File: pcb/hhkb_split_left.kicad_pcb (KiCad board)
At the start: 2 copper layers, 140.4 x 97.4 mm, 74 parts, among them SW1 Esc, SW10 E, SW11 R, SW12 T, SW13 Ctrl, SW14 A, SW15 S, SW16 D, SW17 F, SW18 G, SW19 Shift, SW2 1, SW20 Z, SW21 X, SW22 C, SW23 V, SW24 B, SW25 Alt, SW26 Meta, SW27 L-Space, SW3 2, SW4 3, SW5 4, SW6 5, SW7 Tab, SW8 Q, SW9 W, U1 74LVC595

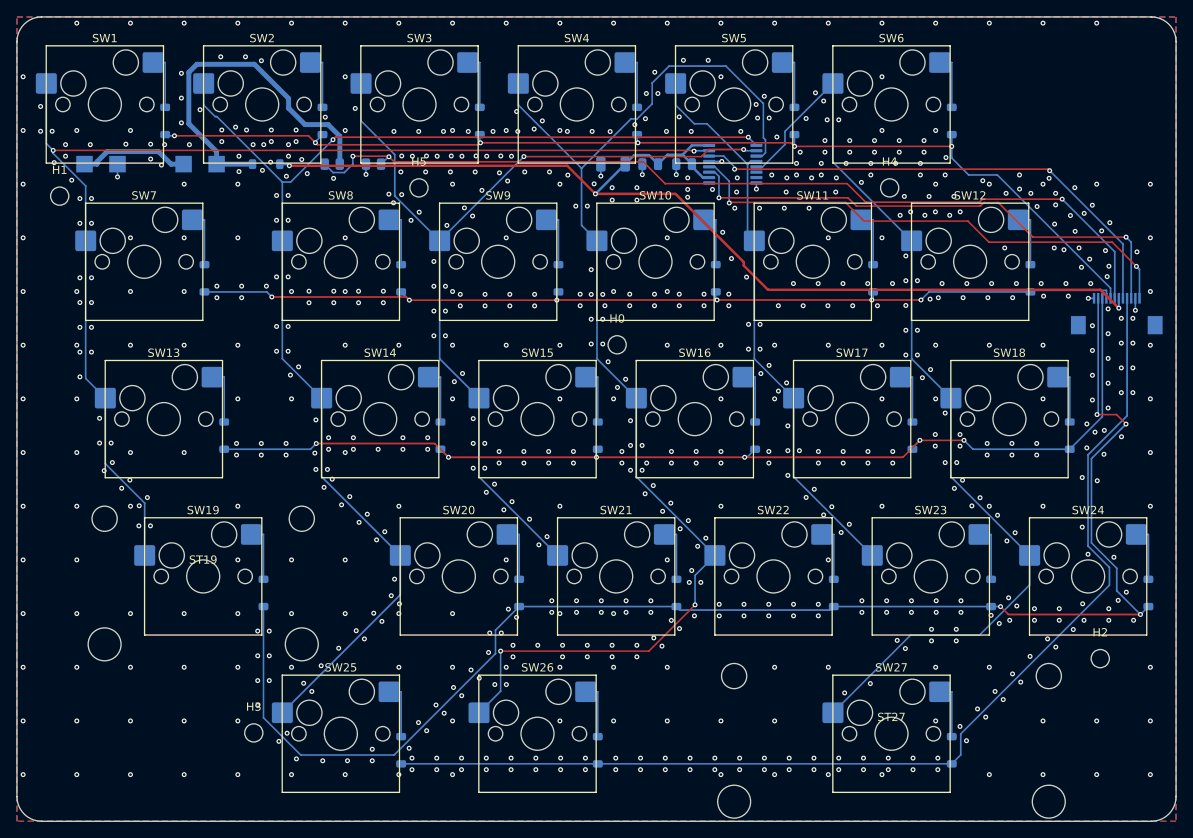
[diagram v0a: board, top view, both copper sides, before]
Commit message: C_RAIL を消した。置き場所の根拠が持たず C_U1 の重複だった
open-gaps #39 は「U1 の隣か J_DB の隣か」で止まっていたが、二択の
立て方が違った。FFC の反対側の C_DB を数えると、U_MCU から 3.95mm の
XIAO 用パスコンで、FFC 入口ではない。つまりケーブル入口のパスコンは
もともと両端どちらにも無く、片端だけ手当てする案は理屈が対称にならない。

C_RAIL は実測で J_DB から 70mm、C_U1 の 5.1mm 隣にあった（J_DB を
帯 1 へ移したときに取り残された）。名前どおりの役目は果たしていない。

消した理由は「不要と証明できたから」ではなく、必要と言える根拠が
1 つも無く、各 IC が既に自分の直近パスコンを持つから（595 は
C_U1/C_U2、XIAO は C_DB、レールは C_BULK）。

DRC 違反は左右子とも 0 のまま。右だけ未配線が 0 → 1 に増えた。中身は
信号線ではなく、(152.65, 68.37) の GND スティッチングビアがベタから
浮いたもの（C_RAIL の跡地）。自動配線 2 回で同じなので構造的。
配線に大きな変更が控えているため、それと併せて確認する（open-gaps #40）。

⚠️ pytest tools は最後まで通していない。次の配線変更とまとめて回す。

Co-Authored-By: Claude Opus 5 (1M context) <noreply@anthropic.com>
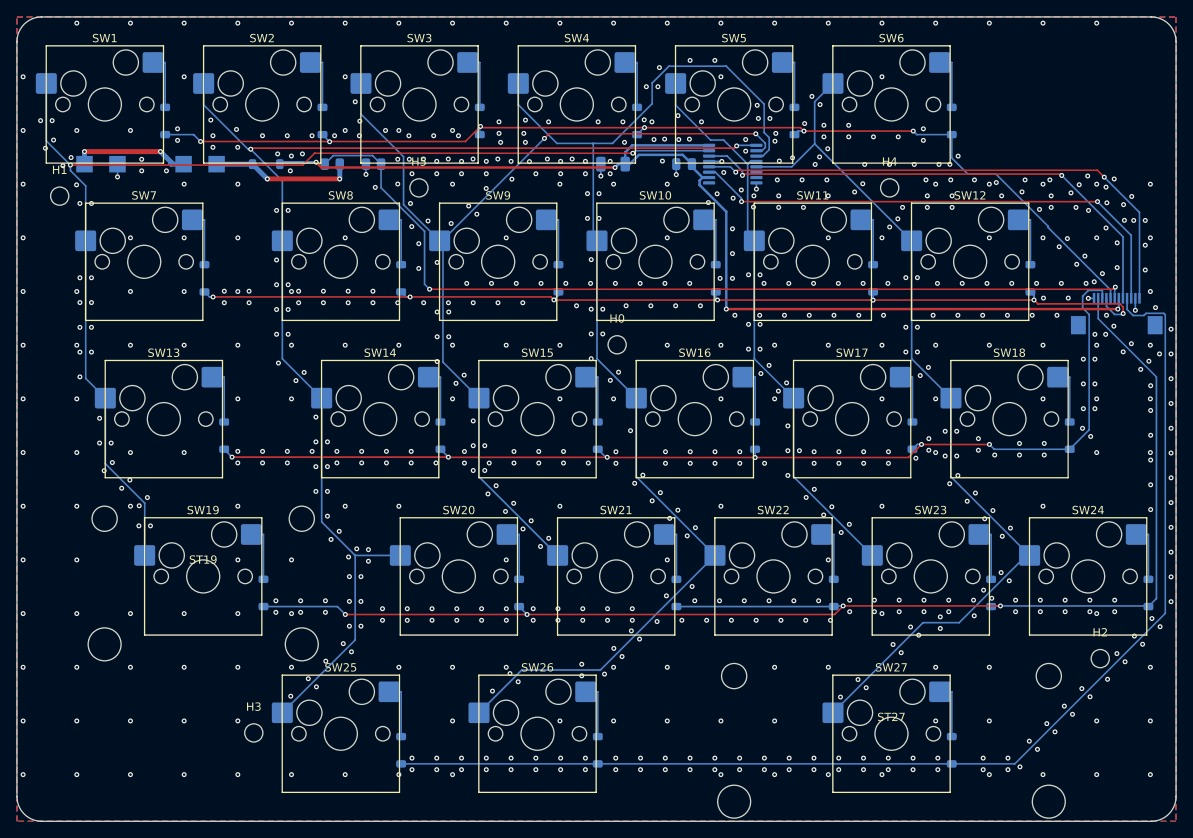
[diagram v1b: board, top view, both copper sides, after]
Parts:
- removed C_RAIL: cap_100n, C_0805_2012Metric
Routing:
- net VBATT_SW: track 43.2 -> 17.4 mm, vias 0 -> 2
- net ROW4: track 134.0 -> 142.7 mm
- net ROW3: track 178.1 -> 171.4 mm
- net COL5: track 115.2 -> 108.6 mm
- net ROW1: track 115.6 -> 122.0 mm, vias 6 -> 7
- net COL3: track 146.2 -> 141.6 mm, vias 2 -> 0
- net COL2: track 110.0 -> 113.9 mm
- net CS: track 62.4 -> 65.0 mm
- net COL1: track 152.2 -> 154.5 mm
- net ROW2: track 130.1 -> 132.4 mm
- net COL0: track 141.6 -> 140.1 mm
- net GND: track 11.2 -> 9.96 mm, vias 817 -> 816
- net SPI_SCK: track 63.3 -> 62.1 mm
- net VBATT_RAW: track 13.4 -> 14.3 mm, vias 0 -> 2
- net SPI_MOSI: track 61.3 -> 62.0 mm
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
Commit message: バルクを子基板へ移し、電源鎖を消費側へ寄せ、行バスを直線にした
利用者の指摘を順に潰した。どれも「測ったら前提が違っていた」型。

1. バルク（C_BULK）を子基板へ
   守る相手は XIAO の µs 級の電流変動（electrical-design 1-5）で、
   595 でも整流点でもない。XIAO は子基板にいるので、主基板に置くと
   FFC 100mm のインダクタンスの外側から供給することになる。
   XIAO の 3V3 パッドから 2.04mm の位置へ移した。

2. 電源ブロックを V3V3 の消費側へ
   整流点 D_PWR が板の左端にあるのに、消費側（C_U1・U1・J_DB）は
   全部反対側だった。U1 の左へ寄せて V3V3 の銅 132→81mm、
   VBATT_SENSE 110→78mm。左の帯 0 はアンテナ禁止域と取付穴で
   分断されていて、プラス側へは出せない（一度出して DRC 13 件）。

3. 行のバスを裏面の直線で自分で引く（prewire_row_bus）
   ROW0 が 222mm・ビア 7 本・区間 54 で表裏を行き来していた。
   同じ行のダイオードの K 側は y が完全に一致し、ライン上に
   スルーホールが無いので直線が引ける（ROW4 は元から 0 ビアだった）。
   左の未配線 1 本（ROW2）はこれで解決した。
   ⚠️ DSN に (autoroute_settings) を足す道は駄目。左が 66 本に壊れた。

4. アンテナの禁止域（30x15mm）を削除
   利用者の「本当にアンテナの真上ですか」で測ったら、覆っていなかった。
     禁止域 y 30.60..45.60 / 基板後端 48.70 / アンテナ 49.50..53.00
   アンテナは基板の後端より 0.80mm 奥（XIAO_OVERHANG 1.8mm の効果）で、
   平面的に基板の外。禁止域は 3.9mm 的を外したまま 450mm² を捨て、
   左の配線を圧迫していた。
   **根拠に挙げられていた検査は存在しなかった。**interface.py は
   test_the_antenna_keepout_actually_covers_the_antenna が照合すると
   書いていたが、その名前の検査はどこにも無い。実在したのは
   「禁止域の中が空か」だけで、位置は誰も見ていなかった。
   代わりに test_the_antenna_clears_the_main_board を置いた
   （XIAO_OVERHANG を 0 にすると落ちることを確認済み）。

   → open-gaps #23 の幾何の証明（アンテナは必ず 4mm 以上 基板の下に
     入る）は、もう成立していない。ただし余裕は 0.80mm しかないので、
     手 0（アルミ箔で RSSI）の価値は残る。#23 の書き直しは次。

残っているもの（次に着手する）:
  右 未配線 3（GND 離島 1 + V3V3 が J_DB へ届かない 2）★機能的な故障
  左 未配線 1（GND 離島）
  違反はどれも 0。自前配線で塞ぐ案は取らない——今は綺麗に引けても
  配置を変えると黙って壊れ、再現性が無い（利用者の判断）。

pytest tools は未実行。

Co-Authored-By: Claude Opus 5 (1M context) <noreply@anthropic.com>
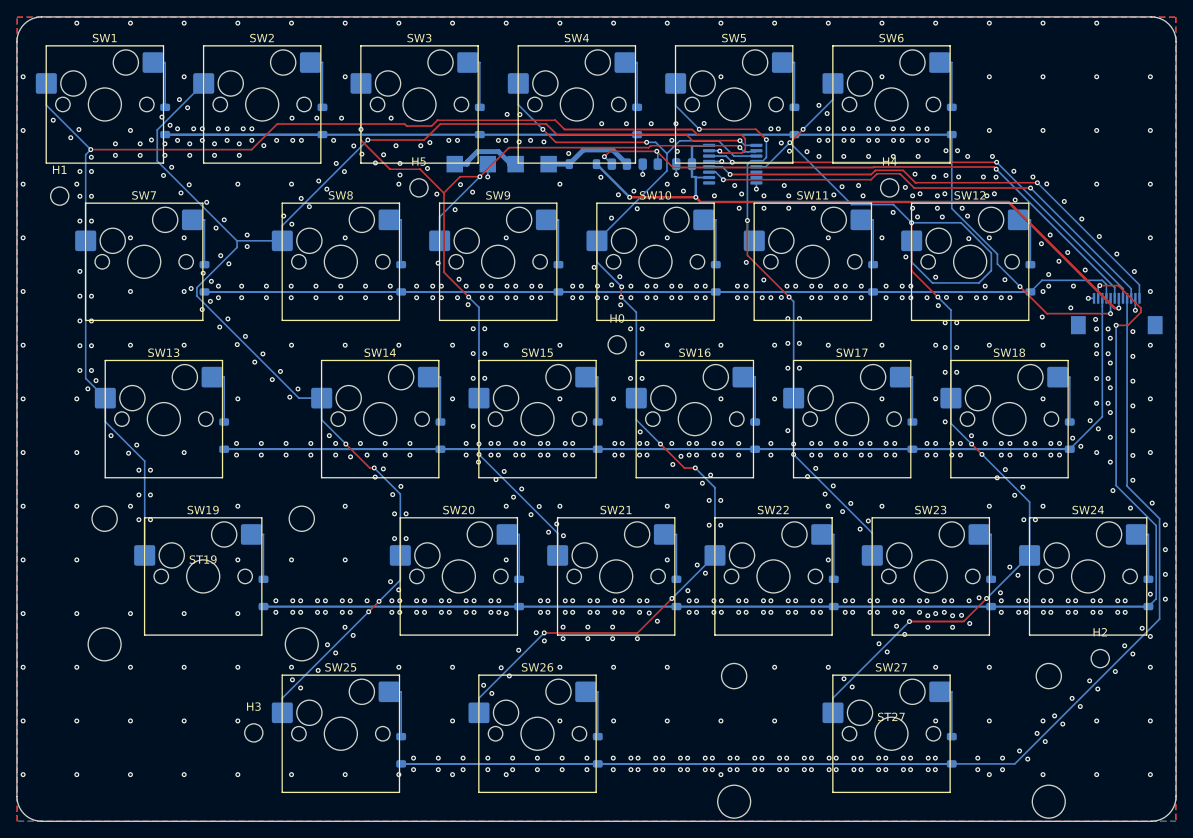
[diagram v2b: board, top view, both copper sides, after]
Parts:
- removed C_BULK: cap_100u, C_1206_3216Metric
- moved BT1_+ 44.8 mm to (132.8, 69.1)
- moved BT1_- 44.8 mm to (136.8, 69.1)
- moved SW_PWR_1 40.2 mm to (140.2, 69.1)
- moved SW_PWR_2 40.2 mm to (144.2, 69.1)
- moved D_PWR 38.3 mm to (148.3, 69.1)
- moved R_HI 34.8 mm to (152.8, 69.1)
- moved R_LO 33.5 mm to (156.5, 69.1)
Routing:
- net ROW0: track 131.4 -> 245.6 mm, vias 6 -> 2
- net ROW2: track 132.4 -> 224.7 mm, vias 6 -> 0
- net ROW3: track 171.4 -> 262.7 mm, vias 4 -> 2
- net ROW1: track 122.0 -> 211.7 mm, vias 7 -> 0
- net ROW4: track 142.7 -> 206.3 mm
- net V3V3: track 132.4 -> 82.1 mm, vias 4 -> 3
- net VBATT_SENSE: track 109.8 -> 73.1 mm, vias 2 -> 3
- net COL5: track 108.6 -> 139.5 mm, vias 0 -> 8
- net COL1: track 154.5 -> 173.5 mm, vias 2 -> 6
- net COL0: track 140.1 -> 150.5 mm
- net COL3: track 141.6 -> 131.7 mm, vias 0 -> 8
- net COL4: track 69.1 -> 76.6 mm, vias 0 -> 6
- net VBATT_SW: track 17.4 -> 10.9 mm, vias 2 -> 0
- net COL2: track 113.9 -> 119.5 mm, vias 2 -> 6
- net VBATT_RAW: track 14.3 -> 8.91 mm, vias 2 -> 0
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
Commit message: VBATT_RAW を廃止し、V3V3 を FFC の隙間を通る幅に直した
1. 電池の + を基板に通さない（利用者の指摘）
   BT1.+ →(VBATT_RAW)→ SW_PWR.1 と基板を往復させていたが、電池
   ボックスもスイッチもリード線で繋ぐので、+ はスイッチへ直接
   はんだ付けすればよい。線 4→3 本・ランド 4→2 個。基板から
   VBATT_RAW というネットが丸ごと消えた。
   ランドの数は WIRE_PAD_KINDS で 2 に決め打ちしていたのを、
   宣言した端子の数から取るように直した。参照名の接尾辞は端子数に
   関わらず付ける（1 個になった瞬間に BT1 へ化けて board_refs と
   回路図の配置表が一斉にずれるため）。

2. V3V3 の線幅 0.3 → 0.2mm ★右の V3V3 断線の真因
   「FFC の 0.30mm パッドに届く必要がある」と書いてあったが、
   **パッドの幅とパッドの隙間を取り違えていた。**0.5mm ピッチ・
   パッド幅 0.30 の列を幅 0.30 で抜けると隣のパッドまで 0.200mm
   ちょうどで、丸めで即割る（0.20mm なら 0.250mm で通る）。
   右基板で V3V3 だけが J_DB から出られず、自動配線器がビアだけ
   (72.75, 84.00) に置いて両端とも繋がず放棄していた。同じ列の
   VBATT_SENSE・SPI_MOSI・SCK・CS は全部 0.20mm で脱出できていた。
   電流は BLE のパルスで 15mA、バルクは子基板側なのでこの線が
   運ぶのは平均電流だけ。0.20mm でも桁が違うほど余る。

3. DSN のクリアランスマージン 15 → 20µm
   上の変更のあと 15 では丸め不足が顕在化し、違反が左 1・右 3 出た
   （実測 0.1917〜0.1919mm ＜ 0.2000mm）。20 で全部消える。
   15/20/25 の結果は autoroute.py に表で残した。

結果:
  左  違反 0 / 未配線 2
  右  違反 0 / 未配線 0   ← 今日はじめて 0/0
  子  違反 0 / 未配線 0

左の 2 本は ROW3/ROW4 が J_DB へ降りる枝。**瑣末と判断**（利用者）。
J_DB の ROW パッドの並び（ROW3,ROW2,ROW1,ROW0,ROW4）が行バスの
y 順と食い違っていて交差する。XIAO のピン割り当てを変えて順序を
揃えれば解ける見込み——次の課題。

pytest tools は未実行。

Co-Authored-By: Claude Opus 5 (1M context) <noreply@anthropic.com>
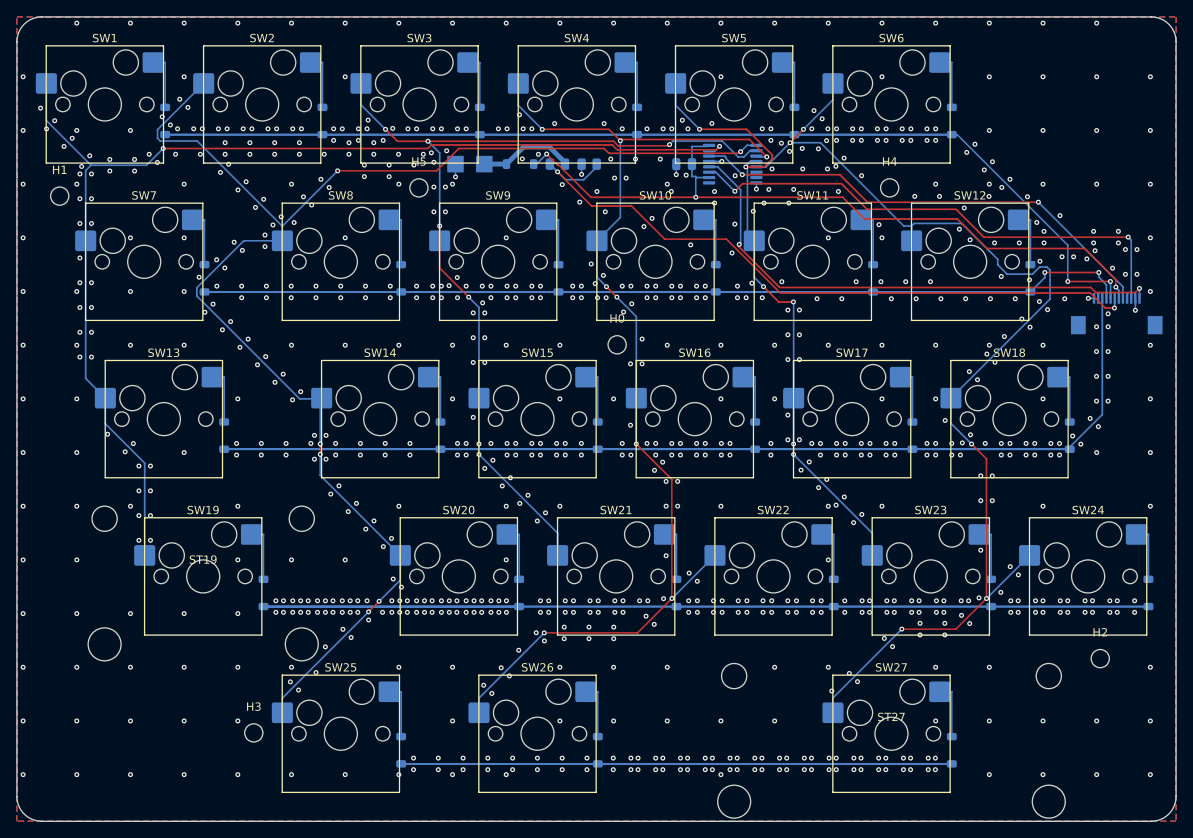
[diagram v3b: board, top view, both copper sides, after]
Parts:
- removed BT1_+: battery_holder, TestPoint_Pad_2.0x2.0mm
- removed SW_PWR_2: wire_pads, TestPoint_Pad_2.0x2.0mm
- moved D_PWR 7.60 mm to (140.8, 69.1)
- moved R_HI 7.50 mm to (145.3, 69.1)
- moved R_LO 7.40 mm to (149.1, 69.1)
- moved BT1_- 3.90 mm to (132.9, 69.1)
- moved SW_PWR_1 3.80 mm to (136.4, 69.1)
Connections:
- SW_PWR_1 pad 1: VBATT_RAW -> VBATT_SW
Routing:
- net ROW4: track 206.3 -> 133.4 mm
- net ROW0: track 245.6 -> 221.7 mm
- net ROW3: track 262.7 -> 245.3 mm, vias 2 -> 0
- net VBATT_SENSE: track 73.1 -> 82.9 mm, vias 3 -> 2
- net VBATT_RAW: track 8.91 -> 0.00 mm
- net COL0: track 150.5 -> 141.6 mm
- net V3V3: track 82.1 -> 90.1 mm
- net COL2: track 119.5 -> 112.3 mm, vias 6 -> 7
- net COL5: track 139.5 -> 134.9 mm, vias 8 -> 5
- net CS: track 60.1 -> 64.1 mm
- net SPI_SCK: track 58.7 -> 62.3 mm
- net COL3: track 131.7 -> 134.6 mm
- net ROW1: track 211.7 -> 213.2 mm, vias 0 -> 2
- net VBATT_SW: track 10.9 -> 11.6 mm
- net COL1: track 173.5 -> 174.2 mm
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
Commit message: 電源を子基板へ移し、FFC のピン順を両基板の都合から決め直した
利用者が絵を見ながら出した指摘を順に潰した回。**私は数字だけ見て
絵を見ておらず、同じ型の見落としを何度も拾ってもらった。**

■ 電源部を子基板へ（open-gaps #41）

  消費者は XIAO で、それは子基板にいる。起動と BLE 初期化で
  2.0〜2.5mA を継続、送信で 10〜15mA のパルス（task-c4-c5 測定 C /
  electrical-design 1-5）。595 の走査 100µA とは 100 倍以上ちがう。
  主基板で整流すると、その mA 級が FFC の 0.2mm 1 本を 100mm 渡る。

    FFC の V3V3   2.0〜2.5mA 継続 + パルス → **約 100µA**（150 分の 1）
    VBATT_SENSE   500kΩ が 100mm 渡る     → **渡らない**（ADC の 2mm 隣）
    ショットキー  隔離点まで FFC 100mm     → **3V3 パッド直近**
    主基板の帯    電源 5 点が SPI を塞ぐ   → **空いた**

  電池もスイッチも子基板のすぐ隣（実測: スイッチ→縁 左 4.0 / 右 20.7mm）
  なのでリード線はむしろ短くなる。

■ FFC のピン順（利用者「DB 単体でなく MAIN の都合も視野に入れて」）

  ROW0/1 は J_DB より上、ROW2/3/4 は下へ伸びる。行番号の昇順に並べると
  上下 2 群が必ず交差する（**実測 3 交差**）。群ごとに近い順で **0 交差**。
  そのズレは **XIAO のピン割り当て＝ファームで吸収**する（利用者の判断
  「配線でひねるのではなくソフトで受けるべき」）。

  ROW4 を D9 から左列へ戻した。右列へ逃がしていた理由は「左列が 6 本だと
  アンテナ直下を 2 本通る」だが、**その 6 本目は VBATT_SENSE だった。**
  分圧が子基板へ移って 5 本に戻ったので前提が消えた。
  → ファームの `&spi2_default`（MISO 外し）が**不要になり削除**。

■ アンテナの禁止域（利用者「こんなに広い必要ある？」「ズレてる」）

  子基板: 幅 18.3mm（XIAO の外形）を使っていた。**アンテナは 3.5mm 角**で
  4.1 倍。さらに y 方向に 2 つの細工（意味の無い切り詰めと水増し）があり、
  **アンテナの 57% しか覆っていなかった**。
    → `antenna_x_band()` に統一。**被覆 100%**、地板の無駄も消えた。
  主基板: アンテナから 3.9mm 外れた場所を抜いて 450mm² を捨てていた。
    → 削除（前のコミット）。

  ⚠️ **SES 往復でルール領域の層が消える**ことを発見した（GetLayer() が -1）。
  層を持たないゾーンは何も禁止しないので、あとから敷いたベタが
  アンテナ直下に入っていた（実測 3297 頂点）。`_restore_rule_area_layers`
  で戻す。**「宣言したから効いている」の 3 回目。**

■ 子基板を主基板と同じ水準に（利用者「MAIN にあって DB に無いもの」）

  両面 GND ベタ（裏面だけだった）・GND ファンアウト・スティッチング・
  離島の救済・電源のネットクラス。順序は **配置 → ネットクラス → 配線 →
  ベタ・ビア**（利用者「ベタは配線の残りで最大限やる」）。
  アンテナの禁止域だけは最初（配置と配線の制約なので）。

■ その他

  - バルクを縦置き＋向きを直した（V3V3/GND が XIAO と平行に並ぶ）
  - 行を D2〜D6 にして D1 を空け、奥側に 2.54mm 作った

■ 検査（どれも故意に壊して落ちることを確認）

  - `test_the_row_order_matches_between_firmware_and_circuit`
    行 N がファームと回路で同じピンを指すか。**既存の検査は集合しか
    見ておらず、D4 と D6 を入れ替えても通っていた**
  - 禁止域の寸法をアンテナの実寸と照合
  - `test_there_is_a_bulk_capacitor` を「XIAO と同じ基板にあるか」に
  - 変異検査が子基板も壊せるように（バルク移設で空振りしていた）
  - 正規表現がゾーンを跨いで**ベタ自身を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
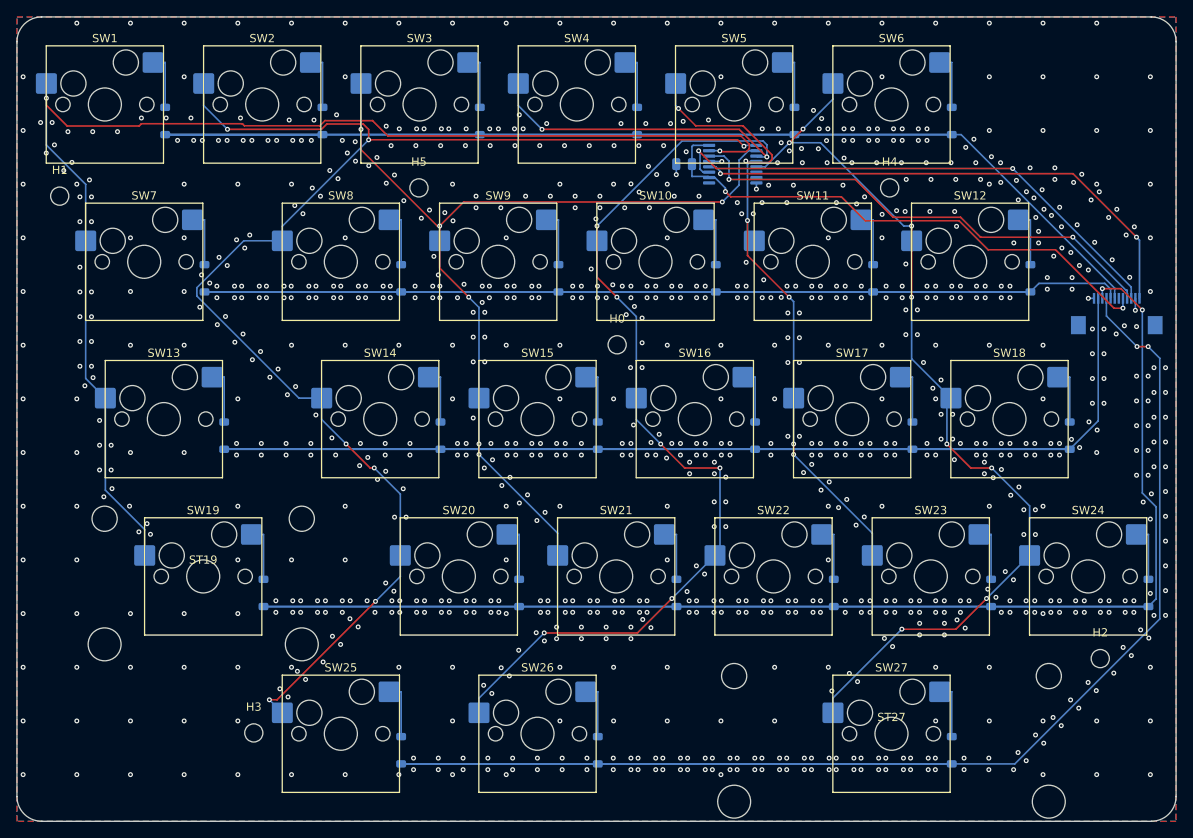
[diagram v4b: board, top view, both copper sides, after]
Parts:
- removed BT1_-: battery_holder, TestPoint_Pad_2.0x2.0mm
- removed D_PWR: schottky, D_SOD-123
- removed R_HI, R_LO: res_1M, R_0805_2012Metric
- removed SW_PWR_1: wire_pads, TestPoint_Pad_2.0x2.0mm
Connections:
- J_DB pad 10: ROW2 -> ROW3
- J_DB pad 11: ROW3 -> ROW2
- J_DB pad 4: ROW4 -> SPI_MOSI
- J_DB pad 5: SPI_MOSI -> V3V3
- J_DB pad 6: V3V3 -> (no net)
- J_DB pad 7: VBATT_SENSE -> ROW0
- J_DB pad 8: ROW0 -> ROW1
- J_DB pad 9: ROW1 -> ROW4
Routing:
- net VBATT_SENSE: track 82.9 -> 0.00 mm, vias 2 -> 0
- net ROW4: track 133.4 -> 208.1 mm, vias 0 -> 2
- net V3V3: track 90.1 -> 66.0 mm, vias 3 -> 2
- net COL5: track 134.9 -> 115.8 mm, vias 5 -> 8
- net COL3: track 134.6 -> 151.3 mm
- net ROW0: track 221.7 -> 238.2 mm, vias 2 -> 0
- net COL0: track 141.6 -> 156.3 mm
- net ROW3: track 245.3 -> 258.4 mm, vias 0 -> 2
- net VBATT_SW: track 11.6 -> 0.00 mm
- net GND: track 8.51 -> 5.71 mm, vias 923 -> 1002
- net COL4: track 77.0 -> 78.8 mm
- net SPI_SCK: track 62.3 -> 64.1 mm
- net ROW1: track 213.2 -> 211.6 mm, vias 2 -> 0
- net SPI_MOSI: track 58.1 -> 59.6 mm
- net CS: track 64.1 -> 63.0 mm
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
